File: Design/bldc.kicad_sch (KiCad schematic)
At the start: 10 parts

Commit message: Restructuring files
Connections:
- net MCU/VBatt renamed MCU/AN_IN_VBatt
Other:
- sheet MCU ports: added AN_IN_VBatt; removed VBatt
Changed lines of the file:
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@@
       (effects (font (size 1.27 1.27)) (justify left top))
     )
-    (pin "VBatt" input (at 83.82 40.64 180)
+    (pin "AN_IN_VBatt" input (at 83.82 40.64 180)
       (effects (font (size 1.27 1.27)) (justify left))
     )

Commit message: schematic updates
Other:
- sheet MCU ports: added CANRX, CANTX, HALLA, HALLB, HALLC, HS_A_TTL, HS_B_TTL, HS_C_TTL, LS_A_TTL, LS_B_TTL, LS_C_TTL, MOTOR_TEMP, PHASEA_FB, PHASEB_FB, PHASEC_FB; removed none
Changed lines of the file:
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@@
+    (stroke (width 0) (type default) (color 0 0 0 0))
+  )
+  (wire (pts (xy 69.85 63.5) (xy 83.82 63.5))
     (stroke (width 0) (type default) (color 0 0 0 0))
   )
@@
     (stroke (width 0) (type default) (color 0 0 0 0))
   )
+  (wire (pts (xy 69.85 60.96) (xy 83.82 60.96))
+    (stroke (width 0) (type default) (color 0 0 0 0))
+  )
   (wire (pts (xy 58.42 47.625) (xy 58.42 43.815))
     (stroke (width 0) (type default) (color 0 0 0 0))
@@
     (stroke (width 0) (type default) (color 0 0 0 0))
   )
+  (wire (pts (xy 69.85 113.03) (xy 83.82 113.03))
+    (stroke (width 0) (type default) (color 0 0 0 0))
+  )
   (wire (pts (xy 35.56 105.41) (xy 39.37 105.41))
     (stroke (width 0) (type default) (color 0 0 0 0))
   )
+  (wire (pts (xy 69.85 68.58) (xy 83.82 68.58))
+    (stroke (width 0) (type default) (color 0 0 0 0))
+  )
   (wire (pts (xy 39.37 118.11) (xy 39.37 120.65))
     (stroke (width 0) (type default) (color 0 0 0 0))
@@
     (stroke (width 0) (type default) (color 0 0 0 0))
   )
+  (wire (pts (xy 69.85 115.57) (xy 83.82 115.57))
+    (stroke (width 0) (type default) (color 0 0 0 0))
+  )
   (wire (pts (xy 27.94 95.25) (xy 39.37 95.25))
     (stroke (width 0) (type default) (color 0 0 0 0))
@@
   )
   (wire (pts (xy 58.42 48.895) (xy 58.42 47.625))
+    (stroke (width 0) (type default) (color 0 0 0 0))
+  )
+  (wire (pts (xy 69.85 66.04) (xy 83.82 66.04))
     (stroke (width 0) (type default) (color 0 0 0 0))
   )
@@
       (effects (font (size 1.27 1.27)) (justify left))
     )
+    (pin "CANRX" input (at 83.82 113.03 180)
+      (effects (font (size 1.27 1.27)) (justify left))
+    )
+    (pin "CANTX" output (at 83.82 115.57 180)
+      (effects (font (size 1.27 1.27)) (justify left))
+    )
+    (pin "HALLB" input (at 83.82 63.5 180)
+      (effects (font (size 1.27 1.27)) (justify left))
+    )
+    (pin "LS_B_TTL" output (at 133.35 51.435 0)
+      (effects (font (size 1.27 1.27)) (justify right))
+    )
+    (pin "LS_C_TTL" output (at 133.35 59.69 0)
+      (effects (font (size 1.27 1.27)) (justify right))
+    )
+    (pin "PHASEC_FB" input (at 133.35 107.95 0)
+      (effects (font (size 1.27 1.27)) (justify right))
+    )
+    (pin "HS_A_TTL" output (at 133.35 41.91 0)
+      (effects (font (size 1.27 1.27)) (justify right))
+    )
+    (pin "HS_B_TTL" output (at 133.35 49.53 0)
+      (effects (font (size 1.27 1.27)) (justify right))
+    )
+    (pin "HS_C_TTL" output (at 133.35 57.785 0)
+      (effects (font (size 1.27 1.27)) (justify right))
+    )
+    (pin "PHASEB_FB" input (at 133.35 105.41 0)
+      (effects (font (size 1.27 1.27)) (justify right))
+    )
+    (pin "HALLA" input (at 83.82 66.04 180)
+      (effects (font (size 1.27 1.27)) (justify left))
+    )
+    (pin "HALLC" input (at 83.82 60.96 180)
+      (effects (font (size 1.27 1.27)) (justify left))
+    )
+    (pin "LS_A_TTL" output (at 133.35 43.815 0)
+      (effects (font (size 1.27 1.27)) (justify right))
+    )
+    (pin "PHASEA_FB" input (at 133.35 102.87 0)
+      (effects (font (size 1.27 1.27)) (justify right))
+    )
+    (pin "MOTOR_TEMP" input (at 83.82 68.58 180)
+      (effects (font (size 1.27 1.27)) (justify left))
+    )
   )
   (sheet (at 148.59 36.83) (size 29.21 46.99) (fields_autoplaced)
@@
   )
   (symbol_instances
+    (path "/3576afc3-3579-4d5a-8fc7-4bb7f2ba81c5/06d1ffd4-f3e7-4a12-ba16-e291ddb1513a"
+      (reference "#GND") (unit 1) (value "GND") (footprint "")
+    )
     (path "/07a796a7-971a-46f8-be0a-5ed59c09f1bb/11afa54f-4732-4e3f-8ea0-f87d2a447e60"
       (reference "#GND") (unit 1) (value "GND") (footprint "")
     )
+    (path "/3576afc3-3579-4d5a-8fc7-4bb7f2ba81c5/1808bb5d-aae3-4c2b-8e6c-461c7f323cc9"
+      (reference "#GND") (unit 1) (value "GND") (footprint "")
+    )
+    (path "/3576afc3-3579-4d5a-8fc7-4bb7f2ba81c5/3635c1db-a2e5-4602-808f-46e56438b001"
+      (reference "#GND") (unit 1) (value "GND") (footprint "")
+    )
+    (path "/3576afc3-3579-4d5a-8fc7-4bb7f2ba81c5/3ae34b80-260d-43fe-a5a6-1a135f36bb3a"
+      (reference "#GND") (unit 1) (value "GND") (footprint "")
+    )
+    (path "/3576afc3-3579-4d5a-8fc7-4bb7f2ba81c5/40913811-dba6-4497-a79f-82f79aae3114"
+      (reference "#GND") (unit 1) (value "GND") (footprint "")
+    )
+    (path "/3576afc3-3579-4d5a-8fc7-4bb7f2ba81c5/45e92be8-6587-4568-82db-45c73c76d2d1"
+      (reference "#GND") (unit 1) (value "GND") (footprint "")
+    )
     (path "/651e52a8-2a4b-4c20-97c5-bfc96d1a6e9c"
       (reference "#GND") (unit 1) (value "GND") (footprint "")
     )
+    (path "/3576afc3-3579-4d5a-8fc7-4bb7f2ba81c5/6a7a57d1-14b9-4e2a-83f9-f8ede2a91a83"
+      (reference "#GND") (unit 1) (value "GND") (footprint "")
+    )
     (path "/07a796a7-971a-46f8-be0a-5ed59c09f1bb/7d6b6dcf-12ee-465f-b098-cfbbff8fdd5e"
       (reference "#GND") (unit 1) (value "GND") (footprint "")
@@
       (reference "#GND") (unit 1) (value "GND") (footprint "")
     )
+    (path "/3576afc3-3579-4d5a-8fc7-4bb7f2ba81c5/9f154282-54ce-4a34-831b-c017c50e5363"
+      (reference "#GND") (unit 1) (value "GND") (footprint "")
+    )
+    (path "/3576afc3-3579-4d5a-8fc7-4bb7f2ba81c5/ae40a51a-8f55-4495-9f47-c30628bca990"
+      (reference "#GND") (unit 1) (value "GND") (footprint "")
+    )
     (path "/07a796a7-971a-46f8-be0a-5ed59c09f1bb/af1cca6a-4931-4bc0-bb4e-4b3cbc366bcb"
+      (reference "#GND") (unit 1) (value "GND") (footprint "")
+    )
+    (path "/3576afc3-3579-4d5a-8fc7-4bb7f2ba81c5/c5651c99-e151-4e9c-a312-bc69f3969460"
+      (reference "#GND") (unit 1) (value "GND") (footprint "")
+    )
+    (path "/3576afc3-3579-4d5a-8fc7-4bb7f2ba81c5/c904f928-4892-4b7f-a9ec-ef59c3ab7a97"
       (reference "#GND") (unit 1) (value "GND") (footprint "")
     )
@@
       (reference "#PWR3.3") (unit 1) (value "+3.3V") (footprint "")
     )
+    (path "/3576afc3-3579-4d5a-8fc7-4bb7f2ba81c5/91ea4670-2c1a-4a79-b753-20121c7551bd"
+      (reference "#PWR3.3") (unit 1) (value "+3.3V") (footprint "")
+    )
     (path "/8ce5b79b-599e-4564-9bf3-d6294bcd3d0e/dbc89416-45cb-4aa8-a6b1-6cfac1d88565"
       (reference "#PWR3.3") (unit 1) (value "+3.3V") (footprint "")
@@
       (reference "#PWR5") (unit 1) (value "+5V") (footprint "")
     )
+    (path "/3576afc3-3579-4d5a-8fc7-4bb7f2ba81c5/88f0ebe2-58b0-4d53-84c4-db86cf73a46a"
+      (reference "#PWR5") (unit 1) (value "+5V") (footprint "")
+    )
     (path "/9d7da0b2-1d74-40ff-8ef8-93ae5ab8b575"
       (reference "#PWR5") (unit 1) (value "+5V") (footprint "")
     )
+    (path "/3576afc3-3579-4d5a-8fc7-4bb7f2ba81c5/9fcbc522-e85b-417a-ac66-e6844e095fa2"
+      (reference "#PWR5") (unit 1) (value "+5V") (footprint "")
+    )
     (path "/0375721a-e006-4524-8e5d-b77dfdd9256f"
       (reference "#PWR?") (unit 1) (value "+BATT") (footprint "")
@@
       (reference "JP?") (unit 1) (value "Jumper") (footprint "")
     )
+    (path "/3576afc3-3579-4d5a-8fc7-4bb7f2ba81c5/62f1274a-e802-4ca6-8820-f2e0d0d6c7c0"
+      (reference "JP?") (unit 1) (value "bit0") (footprint "")
+    )
+    (path "/3576afc3-3579-4d5a-8fc7-4bb7f2ba81c5/e23937f3-1465-49de-a99d-e1accbc3cb4f"
+      (reference "JP?") (unit 1) (value "bit0") (footprint "")
+    )
+    (path "/3576afc3-3579-4d5a-8fc7-4bb7f2ba81c5/242855ed-5f5a-4687-a6bd-4258847ccc6e"
+      (reference "M?") (unit 1) (value "STM32F4-DISCOVERY") (footprint "STM32F4-DISCOVERY-SIMON_STM32F4-DISCOVERY")
+    )
     (path "/07a796a7-971a-46f8-be0a-5ed59c09f1bb/1d61e21e-23e6-43a8-a082-5e0dd70473df"
       (reference "R?") (unit 1) (value "2.2k") (footprint "")
@@
       (reference "R?") (unit 1) (value "10k") (footprint "")
     )
+    (path "/3576afc3-3579-4d5a-8fc7-4bb7f2ba81c5/6e06a1af-47d4-491e-9a0a-bc632358d112"
+      (reference "R?") (unit 1) (value "10k") (footprint "")
+    )
     (path "/07a796a7-971a-46f8-be0a-5ed59c09f1bb/83375e70-c86d-419b-a61d-992bad3f5cb1"
       (reference "R?") (unit 1) (value "2.2k") (footprint "")
     )
+    (path "/3576afc3-3579-4d5a-8fc7-4bb7f2ba81c5/992e3237-abbe-4ebe-8811-fb5ed6f64333"
+      (reference "R?") (unit 1) (value "10k") (footprint "")
+    )
     (path "/d8e264b0-e14f-4860-9f17-d265a3468422"
       (reference "R?") (unit 1) (value "2.2k") (footprint "")
     )
+    (path "/823fda34-25a4-415d-8b6e-532f959c1c21/72ef49ed-4d23-4bdb-9ff0-045e4161bfaa"
+      (reference "U?") (unit 1) (value "UCC2721xA") (footprint "")
+    )
     (path "/8ce5b79b-599e-4564-9bf3-d6294bcd3d0e/940963f3-5f23-4a3f-a25d-2b49ecc5b6c9"
       (reference "U?") (unit 1) (value "TJA1051TK-3") (footprint "Package_DFN_QFN:DFN-8-1EP_3x3mm_P0.65mm_EP1.55x2.4mm")
     )
-  )
+    (path "/823fda34-25a4-415d-8b6e-532f959c1c21/98488c50-4326-4b12-8205-035b91a4460f"
+      (reference "U?") (unit 1) (value "UCC2721xA") (footprint "")
+    )
+    (path "/823fda34-25a4-415d-8b6e-532f959c1c21/bbc4f17c-db1d-4934-adae-2f344a734880"
+      (reference "U?") (unit 1) (value "UCC2721xA") (footprint "")
+    )
+  )

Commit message: MOSFETS
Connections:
- net +5V renamed +3.3V
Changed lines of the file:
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@@
     (pin "1")
   )
-  (symbol (lib_id "power:+5V") (at 39.37 71.12 270) (unit 1)
+  (symbol (lib_id "power:+3.3V") (at 39.37 71.12 270) (unit 1)
     (in_bom yes) (on_board yes)
-    (property "Reference" "#PWR5" (id 0) (at 35.56 71.12 0)
-      (effects (font (size 1.27 1.27)) hide)
-    )
-    (property "Value" "+5V" (id 1) (at 41.91 71.12 90)
+    (property "Reference" "#PWR3.3" (id 0) (at 35.56 71.12 0)
+      (effects (font (size 1.27 1.27)) hide)
+    )
+    (property "Value" "+3.3V" (id 1) (at 41.91 71.12 90)
       (effects (font (size 1.27 1.27)) (justify left))
     )
@@
       (reference "#GND") (unit 1) (value "GND") (footprint "")
     )
-    (path "/8ce5b79b-599e-4564-9bf3-d6294bcd3d0e/3c6d9927-5a3c-41d2-8381-62c1c7f8d260"
-      (reference "#GND?") (unit 1) (value "GND") (footprint "")
-    )
     (path "/07a796a7-971a-46f8-be0a-5ed59c09f1bb/3d11008d-bd60-4069-b165-9b90b7016349"
       (reference "#PWR3.3") (unit 1) (value "+3.3V") (footprint "")
@@
       (reference "#PWR3.3") (unit 1) (value "+3.3V") (footprint "")
     )
+    (path "/9e2ee88e-624b-4335-840c-9e8f12924519"
+      (reference "#PWR3.3") (unit 1) (value "+3.3V") (footprint "")
+    )
     (path "/8ce5b79b-599e-4564-9bf3-d6294bcd3d0e/dbc89416-45cb-4aa8-a6b1-6cfac1d88565"
       (reference "#PWR3.3") (unit 1) (value "+3.3V") (footprint "")
     )
-    (path "/8ce5b79b-599e-4564-9bf3-d6294bcd3d0e/681a0658-b89a-485e-ae61-b33c4f9d501f"
-      (reference "#PWR5") (unit 1) (value "+5V") (footprint "")
-    )
-    (path "/3576afc3-3579-4d5a-8fc7-4bb7f2ba81c5/88f0ebe2-58b0-4d53-84c4-db86cf73a46a"
-      (reference "#PWR5") (unit 1) (value "+5V") (footprint "")
-    )
-    (path "/9d7da0b2-1d74-40ff-8ef8-93ae5ab8b575"
-      (reference "#PWR5") (unit 1) (value "+5V") (footprint "")
-    )
-    (path "/3576afc3-3579-4d5a-8fc7-4bb7f2ba81c5/9fcbc522-e85b-417a-ac66-e6844e095fa2"
-      (reference "#PWR5") (unit 1) (value "+5V") (footprint "")
-    )
     (path "/0375721a-e006-4524-8e5d-b77dfdd9256f"
       (reference "#PWR?") (unit 1) (value "+BATT") (footprint "")
     )
+    (path "/2b5af13a-5cbf-4b8a-8197-5ae9e5a22d4f/0e24a6e5-dc8d-4fba-b457-59f493d55515"
+      (reference "#PWR?") (unit 1) (value "+3.3V") (footprint "")
+    )
     (path "/44116a8f-b185-4f94-a413-67e1bab51f4f"
       (reference "#PWR?") (unit 1) (value "+BATT") (footprint "")
@@
       (reference "#PWR?") (unit 1) (value "GND") (footprint "")
     )
+    (path "/2b5af13a-5cbf-4b8a-8197-5ae9e5a22d4f/548b5d88-5abf-489b-af2a-0f479128e754"
+      (reference "#PWR?") (unit 1) (value "+3.3V") (footprint "")
+    )
+    (path "/2b5af13a-5cbf-4b8a-8197-5ae9e5a22d4f/edff9482-d8c4-497a-92db-3af20abcee4c"
+      (reference "#PWR?") (unit 1) (value "+3.3V") (footprint "")
+    )
     (path "/04c95221-469c-441a-88da-b1b233b6ba4d"
       (reference "C?") (unit 1) (value "100n") (footprint "")
@@
       (reference "C?") (unit 1) (value "2.2u") (footprint "")
     )
+    (path "/2b5af13a-5cbf-4b8a-8197-5ae9e5a22d4f/1e51dd09-2343-48c0-ae62-7bbce8e89869"
+      (reference "C?") (unit 1) (value "2.2u") (footprint "")
+    )
+    (path "/2b5af13a-5cbf-4b8a-8197-5ae9e5a22d4f/223dc2b5-c209-4921-b920-3d7d66287390"
+      (reference "C?") (unit 1) (value "2.2u") (footprint "")
+    )
     (path "/07a796a7-971a-46f8-be0a-5ed59c09f1bb/3de8fd01-2abe-47f6-bf16-57d4802ad08c"
       (reference "C?") (unit 1) (value "4.7nF") (footprint "")
     )
-    (path "/8ce5b79b-599e-4564-9bf3-d6294bcd3d0e/878eb15c-67ff-4558-b257-b639e8f05380"
+    (path "/2b5af13a-5cbf-4b8a-8197-5ae9e5a22d4f/97745c5b-1a44-4005-9740-8a7475b4da4b"
       (reference "C?") (unit 1) (value "2.2u") (footprint "")
     )
@@
       (reference "M?") (unit 1) (value "STM32F4-DISCOVERY") (footprint "STM32F4-DISCOVERY-SIMON_STM32F4-DISCOVERY")
     )
+    (path "/2b5af13a-5cbf-4b8a-8197-5ae9e5a22d4f/039cb29c-b9cc-4200-a803-3bf90fab5d88"
+      (reference "Q?") (unit 1) (value "TPH2R608NH,L1Q") (footprint "")
+    )
+    (path "/2b5af13a-5cbf-4b8a-8197-5ae9e5a22d4f/690d9493-80d3-4f3e-aff2-284f21ad7011"
+      (reference "Q?") (unit 1) (value "TPH2R608NH,L1Q") (footprint "")
+    )
+    (path "/2b5af13a-5cbf-4b8a-8197-5ae9e5a22d4f/6d4c078e-3f02-4dc3-a724-f91643baf54b"
+      (reference "Q?") (unit 1) (value "TPH2R608NH,L1Q") (footprint "")
+    )
+    (path "/2b5af13a-5cbf-4b8a-8197-5ae9e5a22d4f/9b87a2ef-5f26-4e35-b172-18399d076d0b"
+      (reference "Q?") (unit 1) (value "TPH2R608NH,L1Q") (footprint "")
+    )
+    (path "/2b5af13a-5cbf-4b8a-8197-5ae9e5a22d4f/9da2cdcf-87c5-4a47-a676-b726532b6dda"
+      (reference "Q?") (unit 1) (value "TPH2R608NH,L1Q") (footprint "")
+    )
+    (path "/2b5af13a-5cbf-4b8a-8197-5ae9e5a22d4f/a891315a-a40f-49a5-9e6f-6935d8c5f153"
+      (reference "Q?") (unit 1) (value "TPH2R608NH,L1Q") (footprint "")
+    )
+    (path "/2b5af13a-5cbf-4b8a-8197-5ae9e5a22d4f/015cf151-8989-44af-9cc9-b93a20e77cc5"
+      (reference "R?") (unit 1) (value "10") (footprint "")
+    )
     (path "/07a796a7-971a-46f8-be0a-5ed59c09f1bb/1d61e21e-23e6-43a8-a082-5e0dd70473df"
       (reference "R?") (unit 1) (value "2.2k") (footprint "")
@@
       (reference "R?") (unit 1) (value "39k") (footprint "")
     )
+    (path "/2b5af13a-5cbf-4b8a-8197-5ae9e5a22d4f/3f3f0b82-ddda-4ad9-87c0-8d9acbbf6baa"
+      (reference "R?") (unit 1) (value "10k") (footprint "")
+    )
     (path "/07a796a7-971a-46f8-be0a-5ed59c09f1bb/40819226-13b7-42b5-abb0-1beb62326db3"
       (reference "R?") (unit 1) (value "10k") (footprint "")
@@
       (reference "R?") (unit 1) (value "10k") (footprint "")
     )
+    (path "/2b5af13a-5cbf-4b8a-8197-5ae9e5a22d4f/4f6d11e3-e999-4709-98c1-0e0b941f9f95"
+      (reference "R?") (unit 1) (value "10") (footprint "")
+    )
     (path "/07a796a7-971a-46f8-be0a-5ed59c09f1bb/51fb2195-9b45-4ee7-92d3-728da3b9efae"
       (reference "R?") (unit 1) (value "10k") (footprint "")
@@
     (path "/3576afc3-3579-4d5a-8fc7-4bb7f2ba81c5/6e06a1af-47d4-491e-9a0a-bc632358d112"
       (reference "R?") (unit 1) (value "10k") (footprint "")
+    )
+    (path "/2b5af13a-5cbf-4b8a-8197-5ae9e5a22d4f/7d22e8a8-4489-449d-ab11-090a9985b3e3"
+      (reference "R?") (unit 1) (value "10") (footprint "")
     )
     (path "/07a796a7-971a-46f8-be0a-5ed59c09f1bb/83375e70-c86d-419b-a61d-992bad3f5cb1"
       (reference "R?") (unit 1) (value "2.2k") (footprint "")
     )
+    (path "/2b5af13a-5cbf-4b8a-8197-5ae9e5a22d4f/8a0e95cf-fc23-4e72-8135-cbe0b06261c3"
+      (reference "R?") (unit 1) (value "0.0005") (footprint "")
+    )
+    (path "/2b5af13a-5cbf-4b8a-8197-5ae9e5a22d4f/927766d2-842a-4a9f-9ef6-f0f42c837f2b"
+      (reference "R?") (unit 1) (value "10") (footprint "")
+    )
+    (path "/2b5af13a-5cbf-4b8a-8197-5ae9e5a22d4f/989fe818-cd85-4c9a-8e3c-629be1605d84"
+      (reference "R?") (unit 1) (value "10") (footprint "")
+    )
     (path "/3576afc3-3579-4d5a-8fc7-4bb7f2ba81c5/992e3237-abbe-4ebe-8811-fb5ed6f64333"
       (reference "R?") (unit 1) (value "10k") (footprint "")
+    )
+    (path "/2b5af13a-5cbf-4b8a-8197-5ae9e5a22d4f/b1a003c7-13c2-4419-a855-6c7401725f4a"
+      (reference "R?") (unit 1) (value "10k") (footprint "")
+    )
+    (path "/2b5af13a-5cbf-4b8a-8197-5ae9e5a22d4f/b3fb0da6-02fe-4e47-a66d-65e87f786944"
+      (reference "R?") (unit 1) (value "10") (footprint "")
+    )
+    (path "/2b5af13a-5cbf-4b8a-8197-5ae9e5a22d4f/bb104506-48d9-4988-9de3-498826b1290c"
+      (reference "R?") (unit 1) (value "10k") (footprint "")
+    )
+    (path "/2b5af13a-5cbf-4b8a-8197-5ae9e5a22d4f/bee52065-c4ed-4256-9fd7-635c1df899e7"
+      (reference "R?") (unit 1) (value "10k") (footprint "")
+    )
+    (path "/2b5af13a-5cbf-4b8a-8197-5ae9e5a22d4f/c4359296-043c-4a9c-9786-e8897ddea42a"
+      (reference "R?") (unit 1) (value "0.0005") (footprint "")
     )
     (path "/d8e264b0-e14f-4860-9f17-d265a3468422"
       (reference "R?") (unit 1) (value "2.2k") (footprint "")
     )
-    (path "/823fda34-25a4-415d-8b6e-532f959c1c21/72ef49ed-4d23-4bdb-9ff0-045e4161bfaa"
-      (reference "U?") (unit 1) (value "UCC2721xA") (footprint "")
-    )
-    (path "/8ce5b79b-599e-4564-9bf3-d6294bcd3d0e/940963f3-5f23-4a3f-a25d-2b49ecc5b6c9"
-      (reference "U?") (unit 1) (value "TJA1051TK-3") (footprint "Package_DFN_QFN:DFN-8-1EP_3x3mm_P0.65mm_EP1.55x2.4mm")
-    )
-    (path "/823fda34-25a4-415d-8b6e-532f959c1c21/98488c50-4326-4b12-8205-035b91a4460f"
-      (reference "U?") (unit 1) (value "UCC2721xA") (footprint "")
-    )
-    (path "/823fda34-25a4-415d-8b6e-532f959c1c21/bbc4f17c-db1d-4934-adae-2f344a734880"
-      (reference "U?") (unit 1) (value "UCC2721xA") (footprint "")
-    )
-  )
+    (path "/2b5af13a-5cbf-4b8a-8197-5ae9e5a22d4f/ee870477-b08f-4e57-a173-d84f48b9fdf4"
+      (reference "R?") (unit 1) (value "0.0005") (footprint "")
+    )
+    (path "/2b5af13a-5cbf-4b8a-8197-5ae9e5a22d4f/fd594b50-4ef2-42d2-9f3a-c7fc5f627a8a"
+      (reference "R?") (unit 1) (value "10k") (footprint "")
+    )
+    (path "/2b5af13a-5cbf-4b8a-8197-5ae9e5a22d4f/fff08f01-4bdd-4097-baf0-9f60d0237161"
+      (reference "R?") (unit 1) (value "10k") (footprint "")
+    )
+    (path "/2b5af13a-5cbf-4b8a-8197-5ae9e5a22d4f/50ce20ce-80ea-407c-aaa3-3a3c67e4ca15"
+      (reference "U?") (unit 1) (value "AD8418") (footprint "")
+    )
+    (path "/2b5af13a-5cbf-4b8a-8197-5ae9e5a22d4f/8ce8fa83-39ab-4ff7-aad0-7dea3c9514f2"
+      (reference "U?") (unit 1) (value "AD8418") (footprint "")
+    )
+    (path "/2b5af13a-5cbf-4b8a-8197-5ae9e5a22d4f/ded14cd5-ef57-4643-888b-d3a8f2e6156d"
+      (reference "U?") (unit 1) (value "AD8418") (footprint "")
+    )
+    (path "/8ce5b79b-599e-4564-9bf3-d6294bcd3d0e/e46ee0b9-c48c-400e-a8c2-a03765cbd7be"
+      (reference "U?") (unit 1) (value "SN65HVD232") (footprint "Package_SO:SOIC-8_3.9x4.9mm_P1.27mm")
+    )
+  )

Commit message: MOSFETs
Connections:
- net Power MOSFETS/PHASE_C_OUT: now reaches J?.1 (Pin_1)
- net Power MOSFETS/PHASE_B_OUT: now reaches J?.1 (Pin_1)
- net Power MOSFETS/PHASE_A_OUT: now reaches J?.1 (Pin_1)
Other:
- sheet Power MOSFETS ports: added CURR_A, CURR_B, CURR_C, GH_A, GH_B, GH_C, GL_A, GL_B, GL_C, PHASE_A_OUT, PHASE_A_SOURCE, PHASE_B_OUT, PHASE_B_SOURCE, PHASE_C_OUT, PHASE_C_SOURCE; removed none

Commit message: Micro update
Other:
- sheet MCU ports: added NRST, VOLTAGE_A, VOLTAGE_B, VOLTAGE_C; removed none
- note added: "Voltage supply (6V - 50V)"
- note removed: "Voltage supply (8V - 20V)"

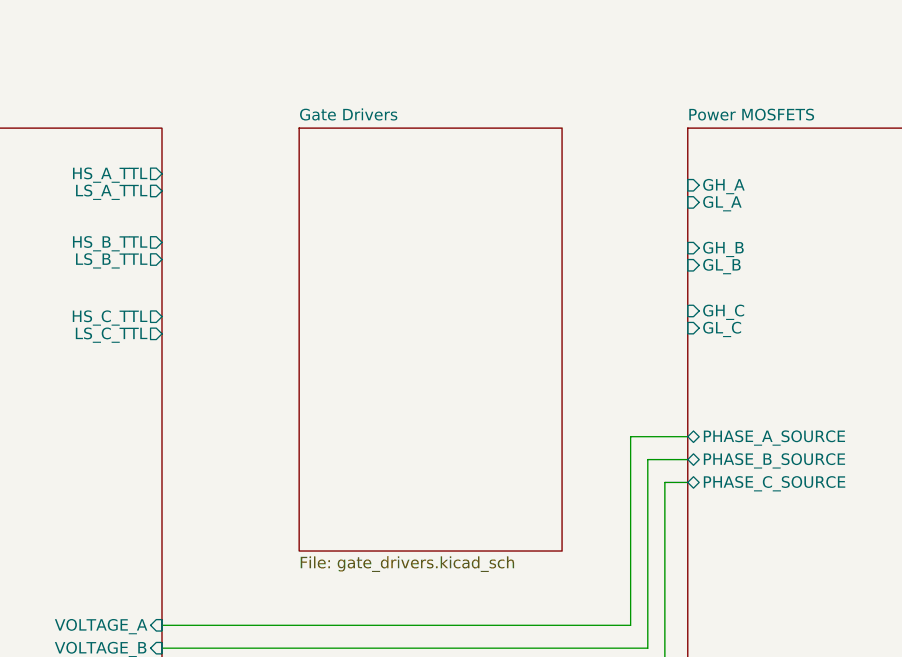
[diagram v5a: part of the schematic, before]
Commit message: gate driver
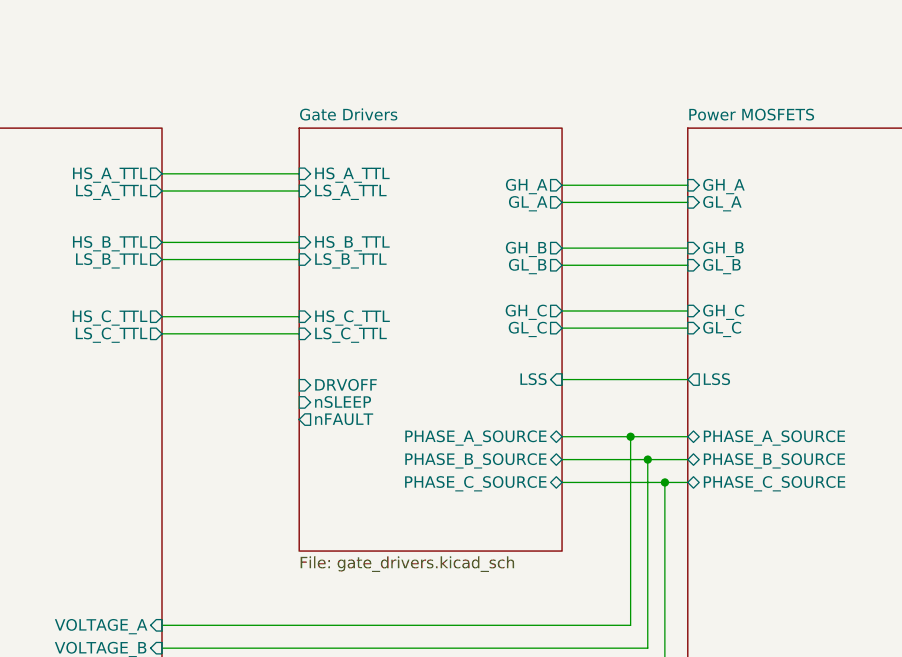
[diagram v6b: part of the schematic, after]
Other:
- sheet Gate Drivers ports: added DRVOFF, GH_A, GH_B, GH_C, GL_A, GL_B, GL_C, HS_A_TTL, HS_B_TTL, HS_C_TTL, LSS, LS_A_TTL, LS_B_TTL, LS_C_TTL, PHASE_A_SOURCE, PHASE_B_SOURCE, PHASE_C_SOURCE, nFAULT, nSLEEP; removed none
- sheet Power MOSFETS ports: added LSS; removed none

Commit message: drv8323RH
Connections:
- net Power MOSFETS/PHASE_A_OUT renamed Gate Drivers/PHASE_A_OUT
- net Power MOSFETS/PHASE_B_OUT renamed Gate Drivers/PHASE_B_OUT
- net Power MOSFETS/PHASE_C_OUT renamed Gate Drivers/PHASE_C_OUT
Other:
- sheet Gate Drivers ports: added CAL, ENABLE, PHASEA_FB, PHASEB_FB, PHASEC_FB, PHASE_A_OUT, PHASE_B_OUT, PHASE_C_OUT, SPA, SPB, SPC; removed DRVOFF, LSS, PHASE_A_SOURCE, PHASE_B_SOURCE, PHASE_C_SOURCE, nSLEEP
- sheet Power MOSFETS ports: added SPA, SPB, SPC; removed CURR_A, CURR_B, CURR_C, LSS, PHASE_A_SOURCE, PHASE_B_SOURCE, PHASE_C_SOURCE
